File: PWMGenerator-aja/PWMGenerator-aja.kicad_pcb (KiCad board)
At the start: 2 copper layers, 29 parts, among them J1 Conn_01x03_Pin, Q1 2N3904, Q2 2N3904, Q3 2N3906, Q4 2N3906, SW1 SW_SPST, U1 LM7805_TO220, U2 LM339

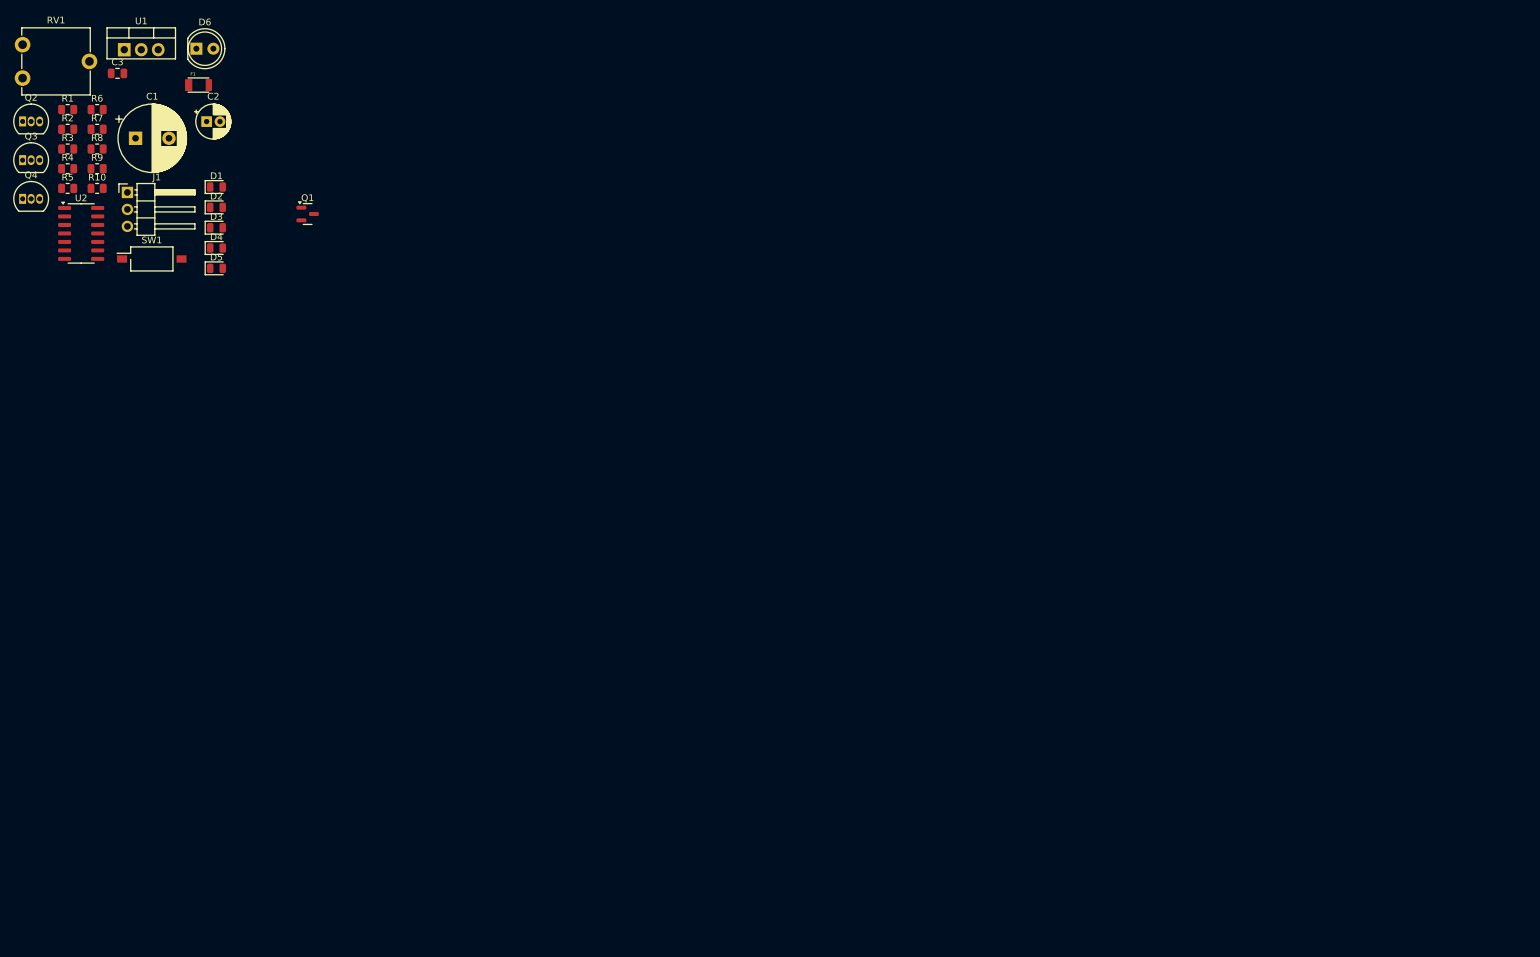
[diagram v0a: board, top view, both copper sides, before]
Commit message: Starting component placement
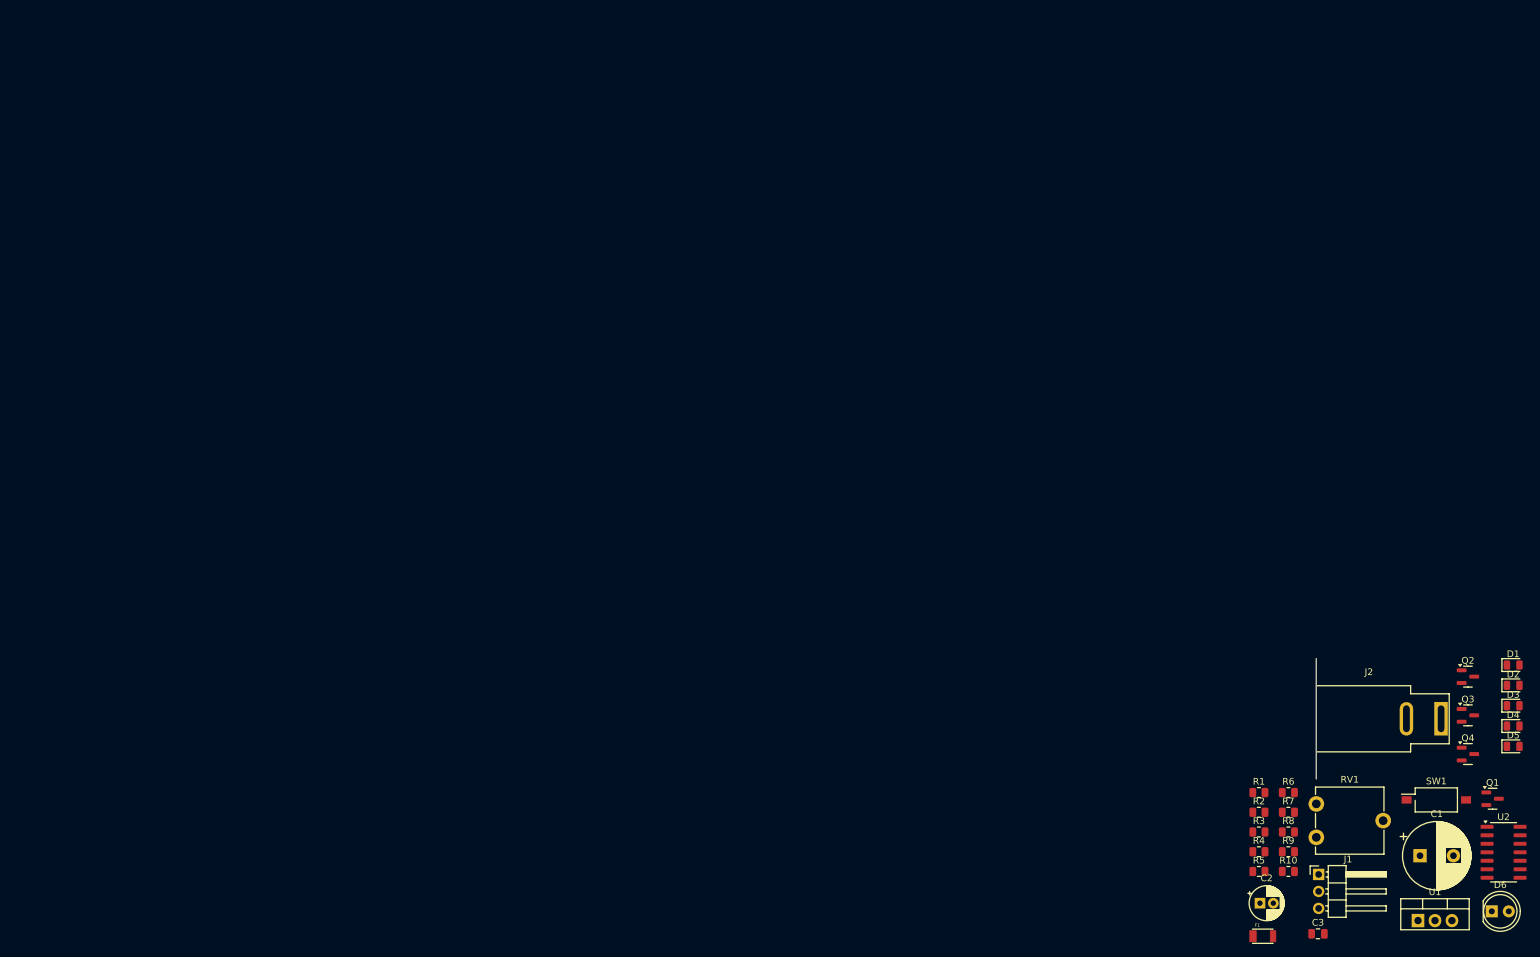
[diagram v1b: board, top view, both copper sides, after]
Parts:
- added J2: Barrel_Jack, Connector_BarrelJack:BarrelJack_SwitchcraftConxall_RAPC10U_Horizontal, F.Cu at (317.4, 55.7)
- F1: footprint local:RESC3115X65N -> lib:RESC3115X65N
- Q2, Q3, Q4: footprint Package_TO_SOT_THT:TO-92_Inline -> Package_TO_SOT_SMD:SOT-23
- moved U1 233.3 mm to (313.9, 85.9)
- moved D6 232.8 mm to (325.0, 84.5)
- moved U2 232.0 mm to (326.7, 75.7)
- moved Q2 231.6 mm to (321.4, 49.4)
- moved Q3 231.6 mm to (321.4, 55.2)
- moved Q4 231.6 mm to (321.4, 61.0)
- moved RV1 224.4 mm to (298.7, 73.4)
- moved C3 220.9 mm to (299.0, 87.9)
- moved C1 220.1 mm to (314.2, 76.2)
- moved SW1 208.5 mm to (316.7, 67.8)
- moved D1 206.7 mm to (328.2, 47.7)
- moved D2 206.7 mm to (328.2, 50.7)
- moved D3 206.7 mm to (328.2, 53.7)
- moved D4 206.7 mm to (328.2, 56.8)
- moved D5 206.7 mm to (328.2, 59.8)
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
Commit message: Work on component placement
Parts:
- moved D6 278.2 mm to (47.2, 68.0)
- moved D2 274.1 mm to (56.0, 83.5)
- moved D1 273.6 mm to (56.0, 76.0)
- moved SW1 268.4 mm to (48.5, 78.5), turned to -90 degrees
- moved D4 266.0 mm to (63.5, 83.5)
- moved D3 265.6 mm to (63.5, 76.0)
- moved J2 260.3 mm to (60.2, 96.0)
- moved D5 257.8 mm to (71.5, 83.5)
- moved Q1 256.7 mm to (70.0, 96.5)
- moved U1 251.1 mm to (63.4, 68.5)
- moved Q2 249.8 mm to (76.1, 96.5)
- moved F1 242.2 mm to (48.5, 86.0)
- moved Q3 242.0 mm to (82.0, 90.5), turned to 90 degrees
- moved U2 237.3 mm to (90.5, 98.3), turned to -90 degrees
- moved C1 236.2 mm to (78.0, 79.0)
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
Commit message: bup
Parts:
- moved J1 13.0 mm to (99.1, 80.5)
- moved C1 12.1 mm to (71.1, 69.0)
- moved Q4 11.8 mm to (88.9, 78.5)
- moved R7 11.8 mm to (77.5, 78.6)
- moved R8 11.8 mm to (82.5, 78.5)
- moved RV1 7.57 mm to (95.5, 71.5)
- moved C2 5.70 mm to (66.0, 75.0)
- moved D1 5.70 mm to (50.5, 74.5)
- moved D2 5.70 mm to (50.5, 82.0)
- moved D3 5.70 mm to (58.0, 74.5)
- moved D4 5.70 mm to (58.0, 82.0)
- moved D5 5.70 mm to (66.0, 82.0)
- moved D6 5.70 mm to (41.7, 66.5)
- moved F1 5.70 mm to (43.0, 84.5)
- moved R3 5.70 mm to (50.5, 66.5)
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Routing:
- net Net-(J1-Pin_2): track 0.00 -> 29.2 mm
- net Net-(U2A-+): track 0.00 -> 23.8 mm
- net GND: track 0.00 -> 21.1 mm, vias 0 -> 4
- net Net-(D3-K): track 0.00 -> 19.6 mm
- net Net-(Q1-C): track 0.00 -> 18.1 mm
- net Net-(Q4-B): track 0.00 -> 15.1 mm
- net Net-(Q1-B): track 0.00 -> 9.32 mm
- net Net-(R9-Pad2): track 0.00 -> 9.21 mm
- net Net-(Q3-B): track 0.00 -> 8.00 mm
- net Net-(Q3-E): track 0.00 -> 6.24 mm
- net Net-(Q2-C): track 0.00 -> 5.62 mm
- added copper zone on B.Cu, net GND
- added copper zone on F.Cu, net VCC
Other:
- board outline added: 81 x 50 mm

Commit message: meh
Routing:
- net Net-(SW1-A): track 0.00 -> 44.2 mm
- net GND: track 21.1 -> 54.4 mm, vias 4 -> 5
- net GNDPWR: track 0.00 -> 31.9 mm
- net Net-(Q2-C): track 5.62 -> 36.1 mm
- net Net-(D5-K): track 0.00 -> 30.1 mm
- net Net-(D1-K): track 0.00 -> 28.5 mm
- net Net-(D3-K): track 19.6 -> 38.6 mm, vias 0 -> 2
- net Net-(U2A-+): track 23.8 -> 42.2 mm
- net Net-(Q3-B): track 8.00 -> 16.7 mm, vias 0 -> 2
- net Net-(D6-A): track 0.00 -> 5.32 mm
- net VAC: track 0.00 -> 3.71 mm
